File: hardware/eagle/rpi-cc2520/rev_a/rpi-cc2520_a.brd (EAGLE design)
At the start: 19.6 x 34 mm, 24 parts, among them P1 MOLEX_73251-135X, U1 CC2520, U2 DS2411, X1 NX2520SA

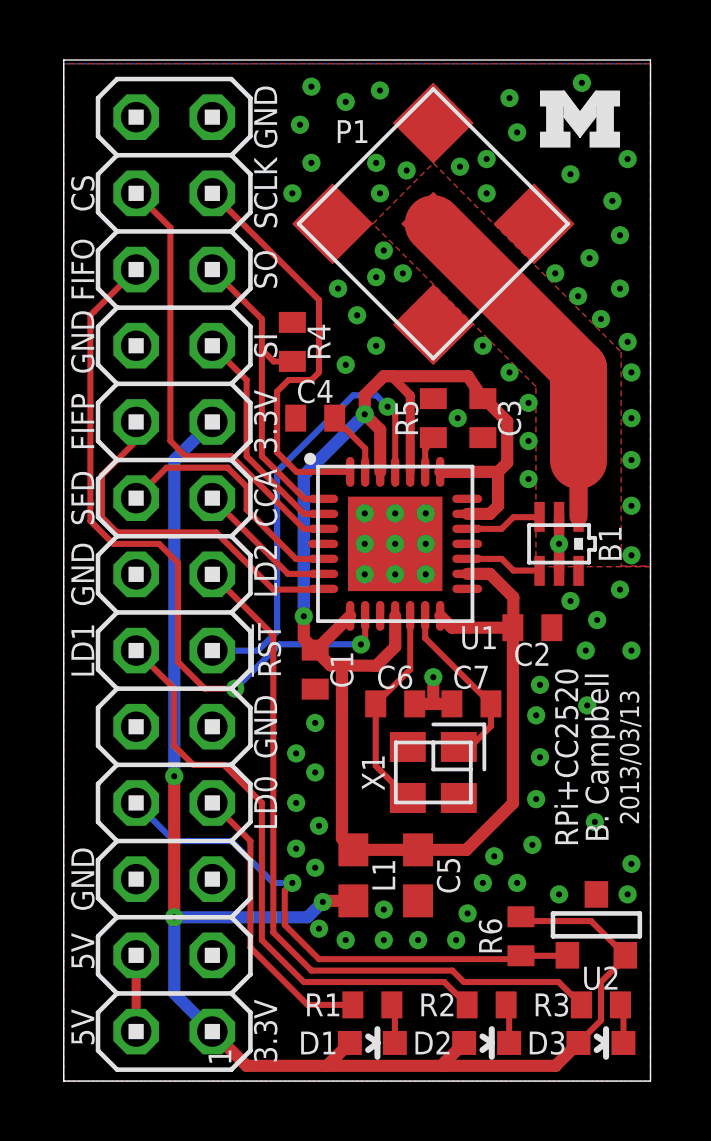
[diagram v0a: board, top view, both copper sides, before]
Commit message: updated rf traces and silkscreen labels
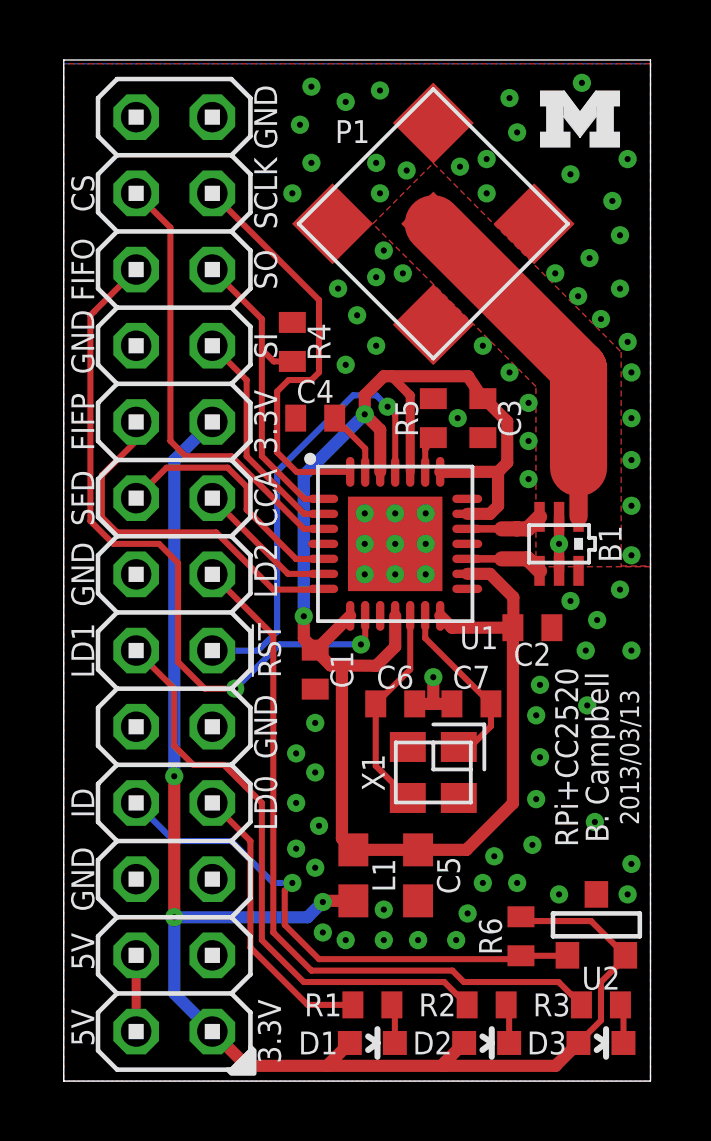
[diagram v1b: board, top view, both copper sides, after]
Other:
- board text added: "ID"
- board text removed: "1"
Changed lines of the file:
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@@
 <wire x1="19.558" y1="34.036" x2="0" y2="34.036" width="0" layer="20"/>
 <wire x1="0" y1="34.036" x2="0" y2="0" width="0" layer="20"/>
-<text x="5.588" y="0.508" size="0.762" layer="21" font="vector" ratio="10" rot="R90">1</text>
 <text x="17.145" y="10.795" size="0.762" layer="21" font="vector" ratio="12" rot="R90" align="bottom-center">RPi+CC2520</text>
 <text x="18.161" y="10.795" size="0.762" layer="21" font="vector" ratio="10" distance="25" rot="R90" align="bottom-center">B. Campbell</text>
 <text x="19.177" y="10.795" size="0.635" layer="21" font="vector" ratio="10" rot="R90" align="bottom-center">2013/03/13</text>
-<text x="6.35" y="1.651" size="0.762" layer="21" font="vector" ratio="10" rot="R90" align="top-center">3.3V</text>
+<text x="6.477" y="1.651" size="0.762" layer="21" font="vector" ratio="10" rot="R90" align="top-center">3.3V</text>
 <text x="1.016" y="1.778" size="0.762" layer="21" font="vector" ratio="10" rot="R90" align="bottom-center">5V</text>
 <text x="6.35" y="4.191" size="0.762" layer="51" font="vector" ratio="10" rot="R90" align="top-center">SDA</text>
@@
 <text x="1.016" y="29.591" size="0.762" layer="21" font="vector" ratio="10" rot="R90" align="bottom-center">CS</text>
 <text x="1.016" y="32.131" size="0.762" layer="51" font="vector" ratio="10" rot="R90" align="bottom-center">CE1</text>
+<text x="1.016" y="9.271" size="0.762" layer="21" font="vector" ratio="10" rot="R90" align="bottom-center">ID</text>
+<polygon width="0.1524" layer="21">
+<vertex x="5.461" y="0.381"/>
+<vertex x="5.588" y="0.254"/>
+<vertex x="6.35" y="0.254"/>
+<vertex x="6.35" y="1.016"/>
+<vertex x="6.223" y="1.143"/>
+<vertex x="6.223" y="1.016"/>
+<vertex x="5.588" y="0.381"/>
+</polygon>
 </plain>
 <attributes>
@@
 <via x="10.668" y="4.699" extent="1-16" drill="0.2032"/>
 <via x="13.97" y="6.604" extent="1-16" drill="0.2032"/>
-<via x="8.509" y="5.08" extent="1-16" drill="0.2032"/>
+<via x="8.636" y="4.953" extent="1-16" drill="0.2032"/>
 <via x="15.875" y="10.795" extent="1-16" drill="0.2032"/>
 <via x="15.748" y="9.398" extent="1-16" drill="0.2032"/>
@@
 <contactref element="U1" pad="17"/>
 <contactref element="B1" pad="4"/>
-<wire x1="13.449" y1="17.407" x2="14.597" y2="17.407" width="0.2032" layer="1"/>
-<wire x1="14.597" y1="17.407" x2="14.986" y2="17.018" width="0.2032" layer="1"/>
-<wire x1="15.849" y1="17.018" x2="14.986" y2="17.018" width="0.2032" layer="1"/>
+<wire x1="13.449" y1="17.407" x2="14.597" y2="17.407" width="0.254" layer="1"/>
 <wire x1="15.849" y1="17.018" x2="15.86" y2="17.007" width="0.1524" layer="1"/>
+<wire x1="14.597" y1="17.407" x2="15.46" y2="17.407" width="0.508" layer="1"/>
+<wire x1="15.46" y1="17.407" x2="15.86" y2="17.007" width="0.508" layer="1"/>
 </signal>
 <signal name="RF_N">
 <contactref element="B1" pad="3"/>
 <contactref element="U1" pad="19"/>
-<wire x1="13.449" y1="18.407" x2="14.597" y2="18.407" width="0.2032" layer="1"/>
-<wire x1="14.597" y1="18.407" x2="14.986" y2="18.796" width="0.2032" layer="1"/>
-<wire x1="14.986" y1="18.796" x2="15.849" y2="18.796" width="0.2032" layer="1"/>
+<wire x1="13.449" y1="18.407" x2="14.597" y2="18.407" width="0.254" layer="1"/>
 <wire x1="15.849" y1="18.796" x2="15.86" y2="18.807" width="0.1524" layer="1"/>
+<wire x1="14.597" y1="18.407" x2="15.105" y2="18.407" width="0.508" layer="1"/>
+<wire x1="15.105" y1="18.407" x2="15.46" y2="18.407" width="0.508" layer="1"/>
+<wire x1="15.46" y1="18.407" x2="15.86" y2="18.807" width="0.508" layer="1"/>
 </signal>
 <signal name="N$7">
@@
 <contactref element="P1" pad="1"/>
 <wire x1="12.319" y1="28.575" x2="17.16" y2="23.734" width="1.905" layer="1"/>
-<wire x1="17.16" y1="23.734" x2="17.16" y2="20.686" width="1.905" layer="1"/>
-<wire x1="17.16" y1="18.807" x2="17.16" y2="20.686" width="0.6096" layer="1"/>
+<wire x1="17.16" y1="23.734" x2="17.16" y2="20.447" width="1.905" layer="1"/>
+<wire x1="17.16" y1="18.807" x2="17.16" y2="20.447" width="0.6096" layer="1"/>
 </signal>
 <signal name="ID_DATA">
@@
 <wire x1="18.657" y1="2.44" x2="18.657" y2="1.27" width="0.2032" layer="1"/>
 </signal>
+<signal name="N$4">
+<wire x1="3.556" y1="0.381" x2="4.572" y2="0.381" width="0" layer="19" extent="1-16"/>
+</signal>
 </signals>
+<errors>
+</errors>
 </board>
 </drawing>

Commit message: cleaning up antenna trace with nice roundedness
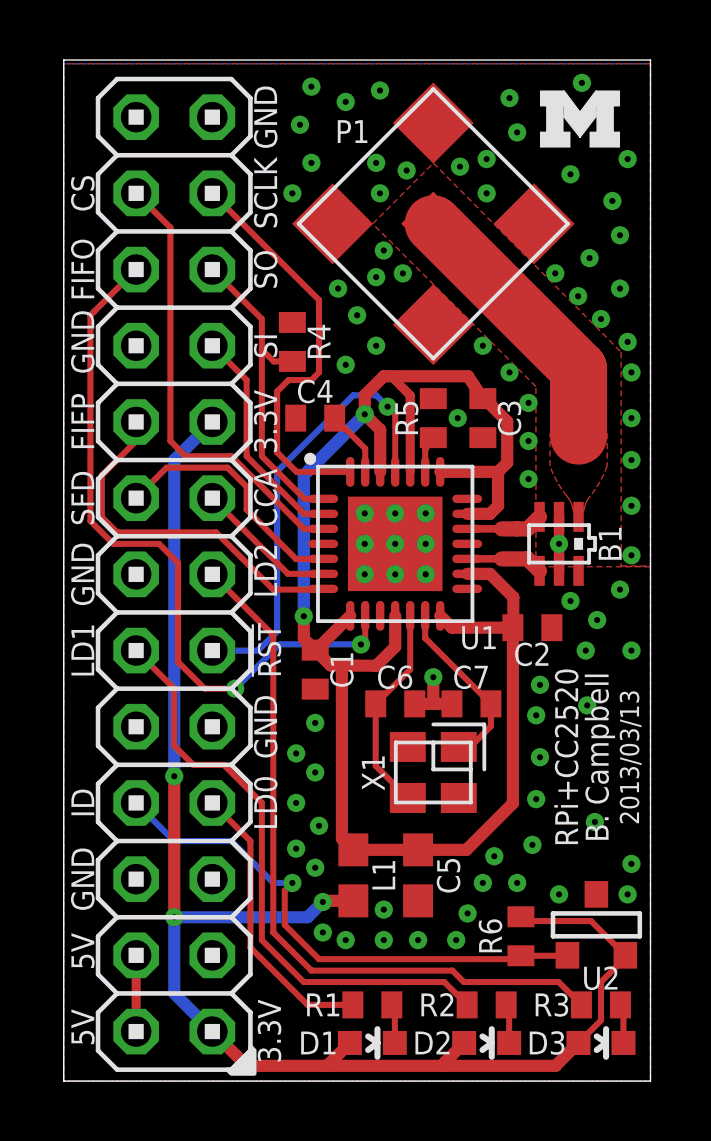
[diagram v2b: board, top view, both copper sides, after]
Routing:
- net N$7: track 11.8 -> 9.08 mm
- added copper zone on layer 1, net N$7
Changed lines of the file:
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@@
 <setting verticaltext="up"/>
 </settings>
-<grid distance="0.1" unitdist="inch" unit="inch" style="lines" multiple="1" display="yes" altdistance="0.005" altunitdist="inch" altunit="inch"/>
+<grid distance="2.54" unitdist="mm" unit="mm" style="lines" multiple="1" display="yes" altdistance="0.005" altunitdist="inch" altunit="inch"/>
 <layers>
 <layer number="1" name="Top" color="4" fill="1" visible="yes" active="yes"/>
@@
 <contactref element="P1" pad="1"/>
 <wire x1="12.319" y1="28.575" x2="17.16" y2="23.734" width="1.905" layer="1"/>
-<wire x1="17.16" y1="23.734" x2="17.16" y2="20.447" width="1.905" layer="1"/>
-<wire x1="17.16" y1="18.807" x2="17.16" y2="20.447" width="0.6096" layer="1"/>
+<wire x1="17.16" y1="23.734" x2="17.16" y2="21.5" width="1.905" layer="1"/>
+<polygon width="0" layer="1" spacing="0.1" thermals="no">
+<vertex x="16.77" y="19.5" curve="-20"/>
+<vertex x="16.2075" y="20.5"/>
+<vertex x="16.2075" y="21.59"/>
+<vertex x="18.1125" y="21.59"/>
+<vertex x="18.1125" y="20.5" curve="-20"/>
+<vertex x="17.55" y="19.5" curve="35"/>
+<vertex x="17.335" y="19"/>
+<vertex x="16.985" y="19" curve="35"/>
+</polygon>
 </signal>
 <signal name="ID_DATA">
@@
 <wire x1="18.657" y1="2.44" x2="18.657" y2="1.27" width="0.2032" layer="1"/>
 </signal>
-<signal name="N$4">
-<wire x1="3.556" y1="0.381" x2="4.572" y2="0.381" width="0" layer="19" extent="1-16"/>
-</signal>
 </signals>
-<errors>
-</errors>
 </board>
 </drawing>

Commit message: more rounding to the rf traces
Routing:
- net RF_P: track 2.59 -> 0.02 mm
- net RF_N: track 2.59 -> 0.02 mm
- added copper zone on layer 1, net RF_N
- added copper zone on layer 1, net RF_P
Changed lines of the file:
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@@
 <setting verticaltext="up"/>
 </settings>
-<grid distance="2.54" unitdist="mm" unit="mm" style="lines" multiple="1" display="yes" altdistance="0.005" altunitdist="inch" altunit="inch"/>
+<grid distance="1" unitdist="mm" unit="mm" style="lines" multiple="1" display="yes" altdistance="0.005" altunitdist="inch" altunit="inch"/>
 <layers>
 <layer number="1" name="Top" color="4" fill="1" visible="yes" active="yes"/>
@@
 <vertex x="19.558" y="0"/>
 <vertex x="19.558" y="17.145"/>
-<vertex x="15.74" y="17.145"/>
+<vertex x="16.383" y="17.145"/>
+<vertex x="16.383" y="16.129"/>
+<vertex x="13.716" y="16.129"/>
+<vertex x="13.716" y="16.891"/>
+<vertex x="12.7" y="16.891"/>
+<vertex x="12.7" y="19.6"/>
+<vertex x="15.74" y="19.6"/>
 <vertex x="15.74" y="23.15"/>
 <vertex x="10.3" y="28.575"/>
@@
 <contactref element="U1" pad="17"/>
 <contactref element="B1" pad="4"/>
-<wire x1="13.449" y1="17.407" x2="14.597" y2="17.407" width="0.254" layer="1"/>
 <wire x1="15.849" y1="17.018" x2="15.86" y2="17.007" width="0.1524" layer="1"/>
-<wire x1="14.597" y1="17.407" x2="15.46" y2="17.407" width="0.508" layer="1"/>
-<wire x1="15.46" y1="17.407" x2="15.86" y2="17.007" width="0.508" layer="1"/>
+<polygon width="0" layer="1" spacing="0.1" thermals="no">
+<vertex x="13.5" y="17.549"/>
+<vertex x="16.04" y="17.549"/>
+<vertex x="16.04" y="16.514"/>
+<vertex x="15.68" y="16.514" curve="50"/>
+<vertex x="14.4" y="17.269"/>
+<vertex x="13.5" y="17.269"/>
+</polygon>
 </signal>
 <signal name="RF_N">
 <contactref element="B1" pad="3"/>
 <contactref element="U1" pad="19"/>
-<wire x1="13.449" y1="18.407" x2="14.597" y2="18.407" width="0.254" layer="1"/>
 <wire x1="15.849" y1="18.796" x2="15.86" y2="18.807" width="0.1524" layer="1"/>
-<wire x1="14.597" y1="18.407" x2="15.105" y2="18.407" width="0.508" layer="1"/>
-<wire x1="15.105" y1="18.407" x2="15.46" y2="18.407" width="0.508" layer="1"/>
-<wire x1="15.46" y1="18.407" x2="15.86" y2="18.807" width="0.508" layer="1"/>
+<polygon width="0" layer="1" spacing="0.1" thermals="no">
+<vertex x="13.5" y="18.545"/>
+<vertex x="14.4" y="18.545" curve="50"/>
+<vertex x="15.68" y="19.3"/>
+<vertex x="16.04" y="19.3"/>
+<vertex x="16.04" y="18.265"/>
+<vertex x="13.5" y="18.265"/>
+</polygon>
+<polygon width="0" layer="1" spacing="0.1" thermals="no">
+<vertex x="13.5" y="18.545"/>
+<vertex x="14.4" y="18.545" curve="50"/>
+<vertex x="15.68" y="19.3"/>
+<vertex x="16.04" y="19.3"/>
+<vertex x="16.04" y="18.265"/>
+<vertex x="13.5" y="18.265"/>
+</polygon>
 </signal>
 <signal name="N$7">
@@
 </signal>
 </signals>
+<errors>
+</errors>
 </board>
 </drawing>
